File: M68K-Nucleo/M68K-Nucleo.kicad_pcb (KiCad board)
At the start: 2 copper layers, 71.1 x 97.8 mm, 20 parts, among them J1 VSel, J2 Current Sense, J3 Conn_01x04, U1 68000D, U2 NUCLEO144-F746ZG, U3 TXB0104D

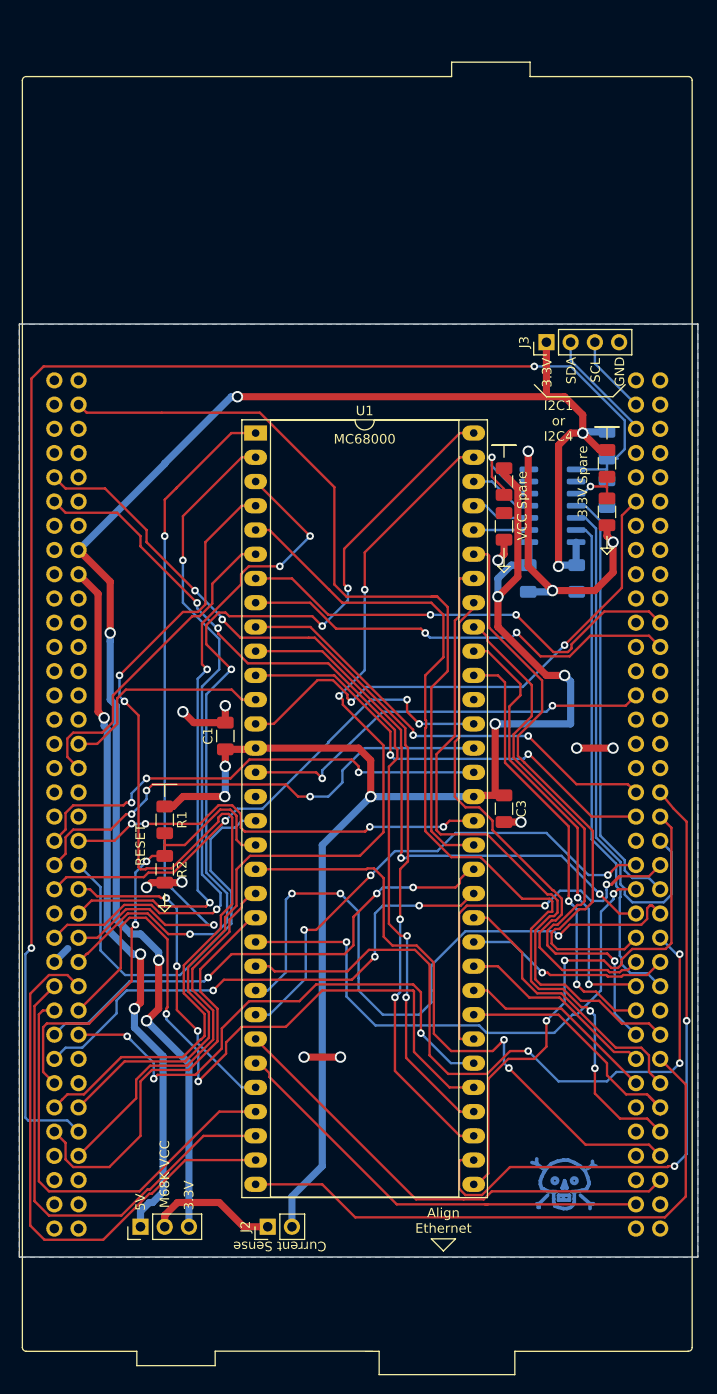
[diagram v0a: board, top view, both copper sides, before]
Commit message: Changed level shifter package on M68k board
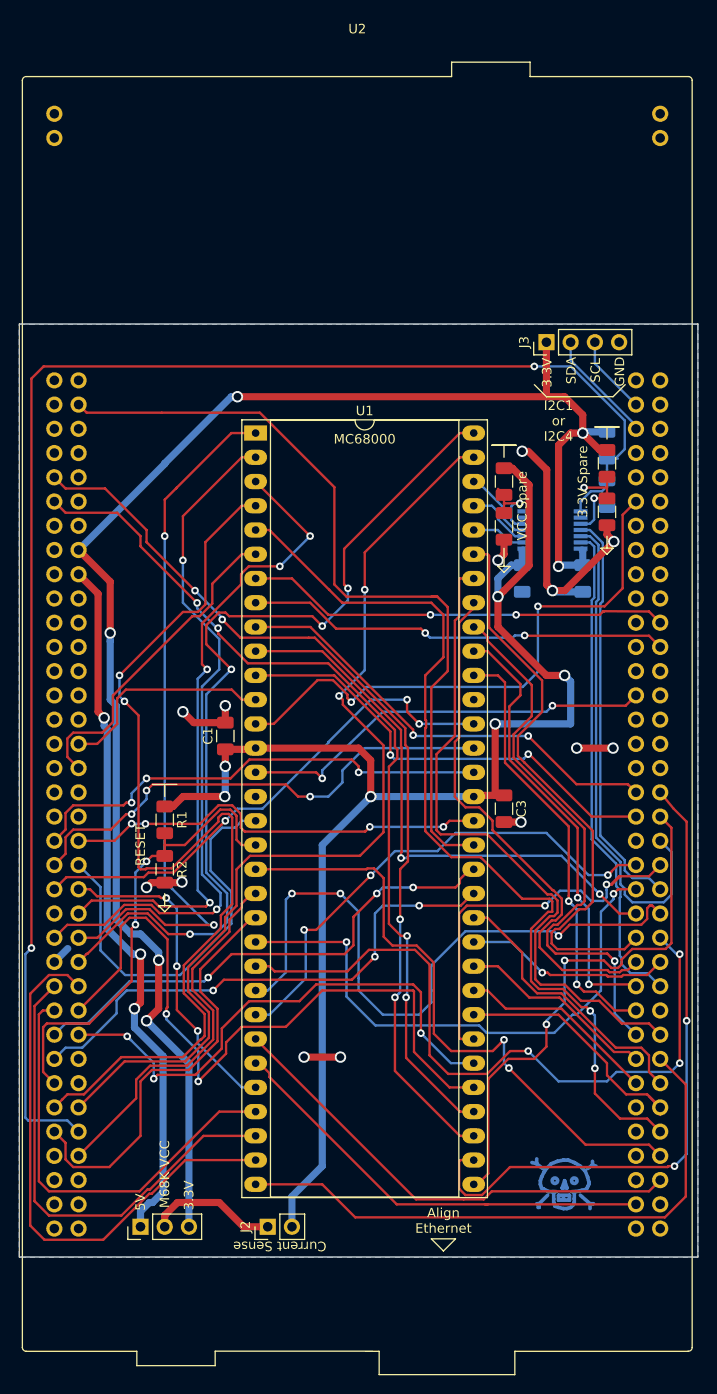
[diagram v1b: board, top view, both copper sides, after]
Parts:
- U2: footprint M68K-Nucleo:ST_Morpho_Connector_144_STLink -> Module:ST_Morpho_Connector_144_STLink
- U3: footprint Package_SO:SOIC-14_3.9x8.7mm_P1.27mm -> Package_SO:TSSOP-14_4.4x5mm_P0.65mm
- moved U3 2.54 mm to (154.9, 80.6)
- moved C2 0.64 mm to (151.8, 85.7)
- moved C4 0.64 mm to (158.1, 85.7)
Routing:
- net /BR: track 56.1 -> 60.2 mm
- net Net-(R7-Pad2): track 6.51 -> 10.5 mm, vias 1 -> 2
- net /UDS: track 48.1 -> 44.7 mm
- net Net-(U2-Pad116): track 45.4 -> 42.9 mm
- net /LDS: track 46.6 -> 44.4 mm
- net Net-(R5-Pad2): track 10.5 -> 8.43 mm
- net Net-(U2-Pad112): track 53.9 -> 52.0 mm
- net Net-(R3-Pad2): track 160.9 -> 162.8 mm
- net Net-(U2-Pad124): track 53.1 -> 51.8 mm
- net GND: track 54.4 -> 53.4 mm
- net VCC: track 151.7 -> 150.8 mm
- net /D7: track 7.23 -> 8.08 mm
- net /D8: track 6.31 -> 7.07 mm
- net +3V3: track 171.3 -> 170.6 mm
